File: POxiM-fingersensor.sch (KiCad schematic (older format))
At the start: 6 parts, among them J1 To LED board, J2 To photodiode board, J3 To readout unit

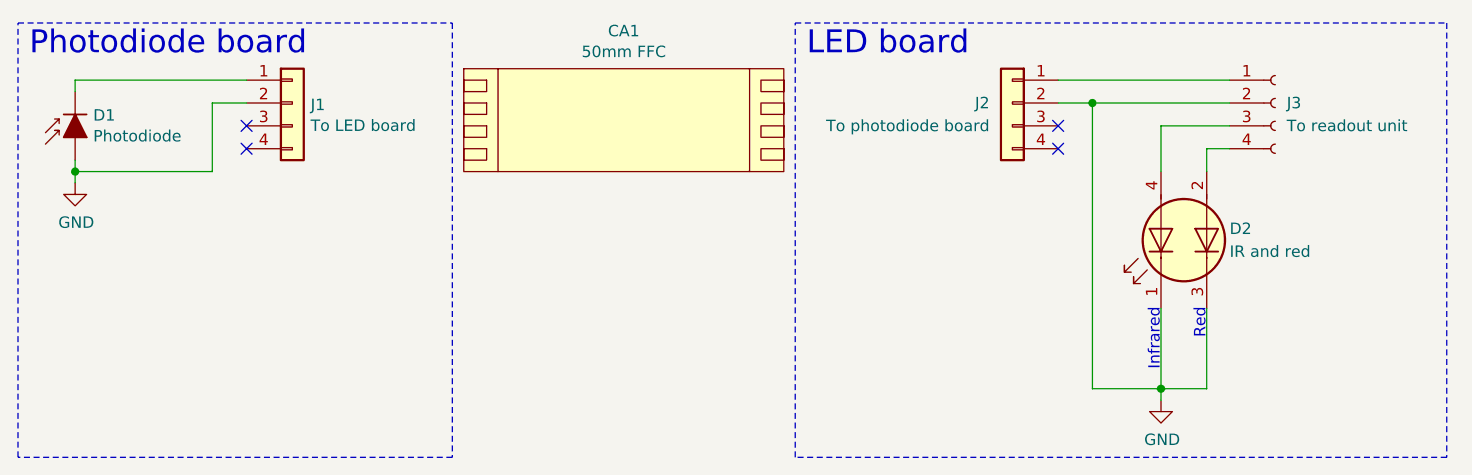
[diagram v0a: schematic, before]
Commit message: Move to flelex layout
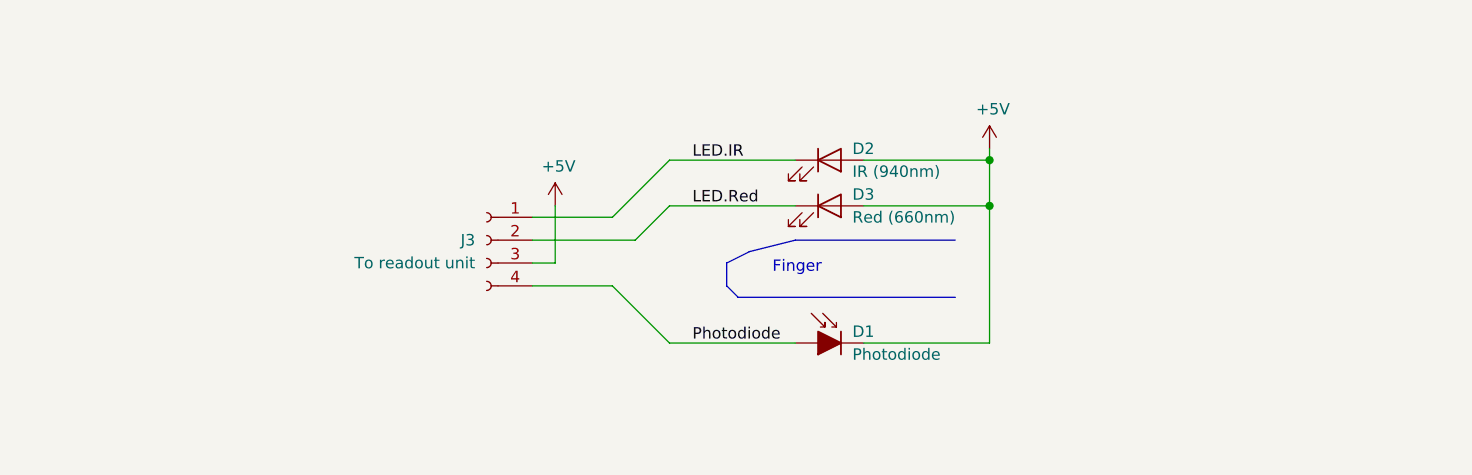
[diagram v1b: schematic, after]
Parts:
- removed CA1: 50mm FFC, POxiM-uncategorised:Accesory, symbol POxiM-mechanical:Premo-Flex_4C
- removed D2: IR and red, POxiM-uncategorised:VSMD66694, symbol POxiM-uncategorised:LED_Dual_AACC
- removed J1: To LED board, POxiM-uncategorised:Molex_200528-0040_1x04-1MP_P1.00mm_Horizontal, symbol Connector_Generic:Conn_01x04
- removed J2: To photodiode board, POxiM-uncategorised:Molex_200528-0040_1x04-1MP_P1.00mm_Horizontal, symbol Connector_Generic:Conn_01x04
- added D2: IR (940nm), LED_SMD:LED_0805_2012Metric, symbol Device:LED
- added D3: Red (660nm), LED_SMD:LED_0805_2012Metric, symbol Device:LED
- J3: footprint POxiM-uncategorised:Molex-Nanofit-4 -> POxiM-uncategorised:Finger-CableConnection; Link https://nl.mouser.com/ProductDetail/Molex/105430-1204?utm_t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 -> (none); Link 2 https://nl.farnell.com/molex/105430-1104/nano-fit-hdr-smt-r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 -> (none); Notes Mouser gold plating, Farnell tin plating -> (none); Order number 538-105430-1204 -> (none); Order number 2 3225233 -> (none); Part number 1054301204 -> (none); Part number 2 105430-1104 -> (none); Supplier Mouser -> (none); Supplier 2 Farnell -> (none)
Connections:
- net LED.IR: now reaches J3.1 (Pin_1)
- net LED.IR: now also D2.1 (K)
- net +5V: now reaches D1.1 (K)
- net +5V: now also J3.3 (Pin_3), D2.2 (A), D3.2 (A)
- net Photodiode: now reaches J3.4 (Pin_4)
- net Photodiode: now also D1.2 (A)
- net GND renamed LED.Red
- net LED.Red: now also D3.1 (K); no longer D1.2 (A)
- no-connect marks 4 -> 0
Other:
- note added: "Finger"
- note removed: "Infrared"
- note removed: "LED board"
- note removed: "Photodiode board"
- note removed: "Red"
- moved on the sheet: D1, J3

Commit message: Export rev F
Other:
- note added: "- Add fudicials\n - Cable connections should have holes in pads\n - Flex part needs to be hatched & no silkscreen\n - Each rigid part needs two 2mm tool holes\n - 0603/0805 agnostic footprints can be used\n - PCB should be less tall\n - Cable connections should be next to LEDs instead of above"
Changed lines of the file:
@@
 Text Label 5800 4450 0    50   ~ 0
 Photodiode
+Text Notes 3150 2550 0    50   ~ 0
+ - Add fudicials\n - Cable connections should have holes in pads\n - Flex part needs to be hatched & no silkscreen\n - Each rigid part needs two 2mm tool holes\n - 0603/0805 agnostic footprints can be used\n - PCB should be less tall\n - Cable connections should be next to LEDs instead of above
 $EndSCHEMATC

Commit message: Rev G
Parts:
- added FID1, FID2, FID3, FID4: Fiducial, Fiducial:Fiducial_0.5mm_Mask1mm, symbol Mechanical:Fiducial
- added H1, H2, H3, H4: M2 alignment hole, MountingHole:MountingHole_2.2mm_M2, symbol Mechanical:MountingHole
- D1: footprint LED_SMD:LED_1206_3216Metric_Castellated -> POxiM-uncategorised:LED_1206_3216Metric_0805_2012Metric_Castellated
- D2, D3: footprint LED_SMD:LED_0805_2012Metric -> POxiM-uncategorised:LED_0805_2012Metric_0603_1608Metric
- J3: Notes (none) -> NOT ON BOM!
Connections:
- net LED.IR: now also D2.2 (A), J3.2 (Pin_2); no longer D2.1 (K), J3.1 (Pin_1)
- net LED.Red: now also D3.2 (A), J3.1 (Pin_1); no longer D3.1 (K), J3.2 (Pin_2)
- net Photodiode: now also D1.1 (K); no longer D1.2 (A)
- removed net +5V: D1.1 (K), D2.2 (A), D3.2 (A), J3.3 (Pin_3)
- new net GND: D1.2 (A), D2.1 (K), D3.1 (K), J3.3 (Pin_3)
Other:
- moved on the sheet: D2, D3
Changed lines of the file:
@@
 L Device:D_Photo_ALT D1
 U 1 1 5EA6D793
-P 6350 4450
-F 0 "D1" H 6200 4500 50  0000 R CNN
-F 1 "Photodiode" H 6200 4400 50  0000 R CNN
-F 2 "LED_SMD:LED_1206_3216Metric_Castellated" H 6300 4450 50  0001 C CNN
-F 3 "${KIPRJMOD}/Datasheets/2711852.pdf" H 6300 4450 50  0001 C CNN
-F 4 "SFH 2701" V 6350 4450 50  0001 C CNN "Part number"
-F 5 "2981719" V 6350 4450 50  0001 C CNN "Order number"
-F 6 "Farnell" V 6350 4450 50  0001 C CNN "Supplier"
-F 7 "" V 6350 4450 50  0001 C CNN "Notes"
-F 8 "https://nl.farnell.com/osram-opto-semiconductors/sfh-2701/photo-diode-820nm-1206/dp/2981719" V 6350 4450 50  0001 C CNN "Link"
-	1    6350 4450
-	-1   0    0    -1
+P 6450 4450
+F 0 "D1" H 6550 4500 50  0000 L CNN
+F 1 "Photodiode" H 6550 4400 50  0000 L CNN
+F 2 "POxiM-uncategorised:LED_1206_3216Metric_0805_2012Metric_Castellated" H 6400 4450 50  0001 C CNN
+F 3 "${KIPRJMOD}/Datasheets/2711852.pdf" H 6400 4450 50  0001 C CNN
+F 4 "SFH 2701" V 6450 4450 50  0001 C CNN "Part number"
+F 5 "2981719" V 6450 4450 50  0001 C CNN "Order number"
+F 6 "Farnell" V 6450 4450 50  0001 C CNN "Supplier"
+F 7 "https://nl.farnell.com/osram-opto-semiconductors/sfh-2701/photo-diode-820nm-1206/dp/2981719" V 6450 4450 50  0001 C CNN "Link"
+	1    6450 4450
+	1    0    0    -1
 $EndComp
 $Comp
@@
 F 2 "POxiM-uncategorised:Finger-CableConnection" H 4900 4000 50  0001 C CNN
 F 3 "~" H 4900 4000 50  0001 C CNN
+F 4 "~" H 0   0   50  0001 C CNN "Link"
+F 5 "NOT ON BOM!" H 0   0   50  0001 C CNN "Notes"
+F 6 "~" H 0   0   50  0001 C CNN "Order number"
+F 7 "~" H 0   0   50  0001 C CNN "Part number"
+F 8 "~" H 0   0   50  0001 C CNN "Supplier"
 	1    4900 4000
 	-1   0    0    -1
@@
 L Device:LED D3
 U 1 1 5EE0E1BF
-P 6400 3850
-F 0 "D3" H 6500 3900 50  0000 L CNN
-F 1 "Red (660nm)" H 6500 3800 50  0000 L CNN
-F 2 "LED_SMD:LED_0805_2012Metric" H 6400 3850 50  0001 C CNN
-F 3 "~" H 6400 3850 50  0001 C CNN
-	1    6400 3850
-	1    0    0    -1
+P 6400 3650
+F 0 "D3" H 6200 3700 50  0000 R CNN
+F 1 "Red (660nm)" H 6200 3600 50  0000 R CNN
+F 2 "POxiM-uncategorised:LED_0805_2012Metric_0603_1608Metric" H 6400 3650 50  0001 C CNN
+F 3 "~" H 6400 3650 50  0001 C CNN
+F 4 "~" H 0   -200 50  0001 C CNN "Link"
+F 5 "~" H 0   -200 50  0001 C CNN "Order number"
+F 6 "~" H 0   -200 50  0001 C CNN "Part number"
+F 7 "~" H 0   -200 50  0001 C CNN "Supplier"
+	1    6400 3650
+	-1   0    0    -1
 $EndComp
 $Comp
 L Device:LED D2
 U 1 1 5EE0E711
-P 6400 3650
-F 0 "D2" H 6500 3700 50  0000 L CNN
-F 1 "IR (940nm)" H 6500 3600 50  0000 L CNN
-F 2 "LED_SMD:LED_0805_2012Metric" H 6400 3650 50  0001 C CNN
-F 3 "~" H 6400 3650 50  0001 C CNN
-	1    6400 3650
-	1    0    0    -1
+P 6400 3850
+F 0 "D2" H 6200 3900 50  0000 R CNN
+F 1 "IR (940nm)" H 6200 3800 50  0000 R CNN
+F 2 "POxiM-uncategorised:LED_0805_2012Metric_0603_1608Metric" H 6400 3850 50  0001 C CNN
+F 3 "~" H 6400 3850 50  0001 C CNN
+F 4 "~" H 0   200 50  0001 C CNN "Link"
+F 5 "~" H 0   200 50  0001 C CNN "Order number"
+F 6 "~" H 0   200 50  0001 C CNN "Part number"
+F 7 "~" H 0   200 50  0001 C CNN "Supplier"
+	1    6400 3850
+	-1   0    0    -1
 $EndComp
 Wire Bus Line
@@
 Wire Wire Line
 	5700 4450 6250 4450
-$Comp
-L power:+5V #PWR0101
-U 1 1 5EE147B5
-P 5200 3850
-F 0 "#PWR0101" H 5200 3700 50  0001 C CNN
-F 1 "+5V" H 5215 4023 50  0000 C CNN
-F 2 "" H 5200 3850 50  0001 C CNN
-F 3 "" H 5200 3850 50  0001 C CNN
-	1    5200 3850
-	1    0    0    -1
-$EndComp
 Wire Wire Line
 	5100 4100 5200 4100
 Wire Wire Line
-	5200 4100 5200 3850
-$Comp
-L power:+5V #PWR0102
-U 1 1 5EE15AC6
-P 7100 3600
-F 0 "#PWR0102" H 7100 3450 50  0001 C CNN
-F 1 "+5V" H 7115 3773 50  0000 C CNN
-F 2 "" H 7100 3600 50  0001 C CNN
-F 3 "" H 7100 3600 50  0001 C CNN
-	1    7100 3600
-	1    0    0    -1
-$EndComp
-Wire Wire Line
-	6550 3650 7100 3650
-Wire Wire Line
-	7100 3650 7100 3850
-Wire Wire Line
-	7100 4450 6550 4450
-Wire Wire Line
-	6550 3850 7100 3850
-Connection ~ 7100 3850
-Wire Wire Line
-	7100 3850 7100 4450
-Wire Wire Line
-	7100 3600 7100 3650
-Connection ~ 7100 3650
+	6550 3650 7200 3650
+Wire Wire Line
+	7200 3650 7200 3850
+Wire Wire Line
+	7200 4450 6550 4450
+Wire Wire Line
+	6550 3850 7200 3850
+Connection ~ 7200 3850
+Wire Wire Line
+	7200 3850 7200 4450
+Text Label 5800 3850 0    50   ~ 0
+LED.IR
 Text Label 5800 3650 0    50   ~ 0
-LED.IR
-Text Label 5800 3850 0    50   ~ 0
 LED.Red
 Text Label 5800 4450 0    50   ~ 0
@@
 Text Notes 3150 2550 0    50   ~ 0
  - Add fudicials\n - Cable connections should have holes in pads\n - Flex part needs to be hatched & no silkscreen\n - Each rigid part needs two 2mm tool holes\n - 0603/0805 agnostic footprints can be used\n - PCB should be less tall\n - Cable connections should be next to LEDs instead of above
+$Comp
+L power:GND #PWR0101
+U 1 1 5F046C3E
+P 5200 4250
+F 0 "#PWR0101" H 5200 4000 50  0001 C CNN
+F 1 "GND" H 5205 4077 50  0000 C CNN
+F 2 "" H 5200 4250 50  0001 C CNN
+F 3 "" H 5200 4250 50  0001 C CNN
+	1    5200 4250
+	1    0    0    -1
+$EndComp
+Wire Wire Line
+	5200 4250 5200 4100
+$Comp
+L power:GND #PWR0102
+U 1 1 5F047B9A
+P 7200 4500
+F 0 "#PWR0102" H 7200 4250 50  0001 C CNN
+F 1 "GND" H 7205 4327 50  0000 C CNN
+F 2 "" H 7200 4500 50  0001 C CNN
+F 3 "" H 7200 4500 50  0001 C CNN
+	1    7200 4500
+	1    0    0    -1
+$EndComp
+Wire Wire Line
+	7200 4500 7200 4450
+Connection ~ 7200 4450
+$Comp
+L Mechanical:MountingHole H1
+U 1 1 5F048FBF
+P 1250 7200
+F 0 "H1" H 1350 7246 50  0000 L CNN
+F 1 "M2 alignment hole" H 1350 7155 50  0000 L CNN
+F 2 "MountingHole:MountingHole_2.2mm_M2" H 1250 7200 50  0001 C CNN
+F 3 "~" H 1250 7200 50  0001 C CNN
+F 4 "~" H 1250 7200 50  0001 C CNN "Part number"
+F 5 "~" H 1250 7200 50  0001 C CNN "Order number"
+F 6 "~" H 1250 7200 50  0001 C CNN "Supplier"
+F 7 "NOT ON BOM!" H 1250 7200 50  0001 C CNN "Notes"
+F 8 "~" H 1250 7200 50  0001 C CNN "Link"
+	1    1250 7200
+	1    0    0    -1
+$EndComp
+$Comp
+L Mechanical:MountingHole H2
+U 1 1 5F049620
+P 1250 7450
+F 0 "H2" H 1350 7496 50  0000 L CNN
+F 1 "M2 alignment hole" H 1350 7405 50  0000 L CNN
+F 2 "MountingHole:MountingHole_2.2mm_M2" H 1250 7450 50  0001 C CNN
+F 3 "~" H 1250 7450 50  0001 C CNN
+F 4 "~" H 1250 7450 50  0001 C CNN "Part number"
+F 5 "~" H 1250 7450 50  0001 C CNN "Order number"
+F 6 "~" H 1250 7450 50  0001 C CNN "Supplier"
+F 7 "NOT ON BOM!" H 1250 7450 50  0001 C CNN "Notes"
+F 8 "~" H 1250 7450 50  0001 C CNN "Link"
+	1    1250 7450
+	1    0    0    -1
+$EndComp
+$Comp
+L Mechanical:MountingHole H3
+U 1 1 5F049B3D
+P 2250 7200
+F 0 "H3" H 2350 7246 50  0000 L CNN
+F 1 "M2 alignment hole" H 2350 7155 50  0000 L CNN
+F 2 "MountingHole:MountingHole_2.2mm_M2" H 2250 7200 50  0001 C CNN
+F 3 "~" H 2250 7200 50  0001 C CNN
+F 4 "~" H 2250 7200 50  0001 C CNN "Part number"
+F 5 "~" H 2250 7200 50  0001 C CNN "Order number"
+F 6 "~" H 2250 7200 50  0001 C CNN "Supplier"
+F 7 "NOT ON BOM!" H 2250 7200 50  0001 C CNN "Notes"
+F 8 "~" H 2250 7200 50  0001 C CNN "Link"
+	1    2250 7200
+	1    0    0    -1
+$EndComp
+$Comp
+L Mechanical:MountingHole H4
+U 1 1 5F04A2B3
+P 2250 7450
+F 0 "H4" H 2350 7496 50  0000 L CNN
+F 1 "M2 alignment hole" H 2350 7405 50  0000 L CNN
+F 2 "MountingHole:MountingHole_2.2mm_M2" H 2250 7450 50  0001 C CNN
+F 3 "~" H 2250 7450 50  0001 C CNN
+F 4 "~" H 2250 7450 50  0001 C CNN "Part number"
+F 5 "~" H 2250 7450 50  0001 C CNN "Order number"
+F 6 "~" H 2250 7450 50  0001 C CNN "Supplier"
+F 7 "NOT ON BOM!" H 2250 7450 50  0001 C CNN "Notes"
+F 8 "~" H 2250 7450 50  0001 C CNN "Link"
+	1    2250 7450
+	1    0    0    -1
+$EndComp
+$Comp
+L Mechanical:Fiducial FID1
+U 1 1 5F04B929
+P 3250 7200
+F 0 "FID1" H 3335 7246 50  0000 L CNN
+F 1 "Fiducial" H 3335 7155 50  0000 L CNN
+F 2 "Fiducial:Fiducial_0.5mm_Mask1mm" H 3250 7200 50  0001 C CNN
+F 3 "~" H 3250 7200 50  0001 C CNN
+F 4 "~" H 0   0   50  0001 C CNN "Link"
+F 5 "NOT ON BOM!" H 0   0   50  0001 C CNN "Notes"
+F 6 "~" H 0   0   50  0001 C CNN "Order number"
+F 7 "~" H 0   0   50  0001 C CNN "Part number"
+F 8 "~" H 0   0   50  0001 C CNN "Supplier"
+	1    3250 7200
+	1    0    0    -1
+$EndComp
+$Comp
+L Mechanical:Fiducial FID2
+U 1 1 5F04C457
+P 3250 7450
+F 0 "FID2" H 3335 7496 50  0000 L CNN
+F 1 "Fiducial" H 3335 7405 50  0000 L CNN
+F 2 "Fiducial:Fiducial_0.5mm_Mask1mm" H 3250 7450 50  0001 C CNN
+F 3 "~" H 3250 7450 50  0001 C CNN
+F 4 "~" H 0   0   50  0001 C CNN "Link"
+F 5 "NOT ON BOM!" H 0   0   50  0001 C CNN "Notes"
+F 6 "~" H 0   0   50  0001 C CNN "Order number"
+F 7 "~" H 0   0   50  0001 C CNN "Part number"
+F 8 "~" H 0   0   50  0001 C CNN "Supplier"
+	1    3250 7450
+	1    0    0    -1
+$EndComp
+$Comp
+L Mechanical:Fiducial FID3
+U 1 1 5F04D55D
+P 3850 7200
+F 0 "FID3" H 3935 7246 50  0000 L CNN
+F 1 "Fiducial" H 3935 7155 50  0000 L CNN
+F 2 "Fiducial:Fiducial_0.5mm_Mask1mm" H 3850 7200 50  0001 C CNN
+F 3 "~" H 3850 7200 50  0001 C CNN
+F 4 "~" H 0   0   50  0001 C CNN "Link"
+F 5 "NOT ON BOM!" H 0   0   50  0001 C CNN "Notes"
+F 6 "~" H 0   0   50  0001 C CNN "Order number"
+F 7 "~" H 0   0   50  0001 C CNN "Part number"
+F 8 "~" H 0   0   50  0001 C CNN "Supplier"
+	1    3850 7200
+	1    0    0    -1
+$EndComp
+$Comp
+L Mechanical:Fiducial FID4
+U 1 1 5F04D563
+P 3850 7450
+F 0 "FID4" H 3935 7496 50  0000 L CNN
+F 1 "Fiducial" H 3935 7405 50  0000 L CNN
+F 2 "Fiducial:Fiducial_0.5mm_Mask1mm" H 3850 7450 50  0001 C CNN
+F 3 "~" H 3850 7450 50  0001 C CNN
+F 4 "~" H 0   0   50  0001 C CNN "Link"
+F 5 "NOT ON BOM!" H 0   0   50  0001 C CNN "Notes"
+F 6 "~" H 0   0   50  0001 C CNN "Order number"
+F 7 "~" H 0   0   50  0001 C CNN "Part number"
+F 8 "~" H 0   0   50  0001 C CNN "Supplier"
+	1    3850 7450
+	1    0    0    -1
+$EndComp
 $EndSCHEMATC

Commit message: Rev I
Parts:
- FID1, FID2, FID3, FID4: footprint Fiducial:Fiducial_0.5mm_Mask1mm -> POxiM-uncategorised:Fiducial_1mm_Mask2mm
- H1, H2, H3, H4: footprint MountingHole:MountingHole_2.2mm_M2 -> POxiM-uncategorised:AlignmentHole_2mm
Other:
- note added: "- Update footprints\n- Tool holes to 2mm\n- Routing posts can extend past board edge\n- Increase fiducial size"
- note removed: "- Add fudicials\n - Cable connections should have holes in pads\n - Flex part needs to be hatched & no silkscreen\n - Each rigid part needs two 2mm tool holes\n - 0603/0805 agnostic footprints can be used\n - PCB should be less tall\n - Cable connections should be next to LEDs instead of above"
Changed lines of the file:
@@
 Photodiode
 Text Notes 3150 2550 0    50   ~ 0
- - Add fudicials\n - Cable connections should have holes in pads\n - Flex part needs to be hatched & no silkscreen\n - Each rigid part needs two 2mm tool holes\n - 0603/0805 agnostic footprints can be used\n - PCB should be less tall\n - Cable connections should be next to LEDs instead of above
+- Update footprints\n- Tool holes to 2mm\n- Routing posts can extend past board edge\n- Increase fiducial size
 $Comp
 L power:GND #PWR0101
@@
 F 0 "H1" H 1350 7246 50  0000 L CNN
 F 1 "M2 alignment hole" H 1350 7155 50  0000 L CNN
-F 2 "MountingHole:MountingHole_2.2mm_M2" H 1250 7200 50  0001 C CNN
+F 2 "POxiM-uncategorised:AlignmentHole_2mm" H 1250 7200 50  0001 C CNN
 F 3 "~" H 1250 7200 50  0001 C CNN
 F 4 "~" H 1250 7200 50  0001 C CNN "Part number"
@@
 F 0 "H2" H 1350 7496 50  0000 L CNN
 F 1 "M2 alignment hole" H 1350 7405 50  0000 L CNN
-F 2 "MountingHole:MountingHole_2.2mm_M2" H 1250 7450 50  0001 C CNN
+F 2 "POxiM-uncategorised:AlignmentHole_2mm" H 1250 7450 50  0001 C CNN
 F 3 "~" H 1250 7450 50  0001 C CNN
 F 4 "~" H 1250 7450 50  0001 C CNN "Part number"
@@
 F 0 "H3" H 2350 7246 50  0000 L CNN
 F 1 "M2 alignment hole" H 2350 7155 50  0000 L CNN
-F 2 "MountingHole:MountingHole_2.2mm_M2" H 2250 7200 50  0001 C CNN
+F 2 "POxiM-uncategorised:AlignmentHole_2mm" H 2250 7200 50  0001 C CNN
 F 3 "~" H 2250 7200 50  0001 C CNN
 F 4 "~" H 2250 7200 50  0001 C CNN "Part number"
@@
 F 0 "H4" H 2350 7496 50  0000 L CNN
 F 1 "M2 alignment hole" H 2350 7405 50  0000 L CNN
-F 2 "MountingHole:MountingHole_2.2mm_M2" H 2250 7450 50  0001 C CNN
+F 2 "POxiM-uncategorised:AlignmentHole_2mm" H 2250 7450 50  0001 C CNN
 F 3 "~" H 2250 7450 50  0001 C CNN
 F 4 "~" H 2250 7450 50  0001 C CNN "Part number"
@@
 F 0 "FID1" H 3335 7246 50  0000 L CNN
 F 1 "Fiducial" H 3335 7155 50  0000 L CNN
-F 2 "Fiducial:Fiducial_0.5mm_Mask1mm" H 3250 7200 50  0001 C CNN
+F 2 "POxiM-uncategorised:Fiducial_1mm_Mask2mm" H 3250 7200 50  0001 C CNN
 F 3 "~" H 3250 7200 50  0001 C CNN
 F 4 "~" H 0   0   50  0001 C CNN "Link"
@@
 F 0 "FID2" H 3335 7496 50  0000 L CNN
 F 1 "Fiducial" H 3335 7405 50  0000 L CNN
-F 2 "Fiducial:Fiducial_0.5mm_Mask1mm" H 3250 7450 50  0001 C CNN
+F 2 "POxiM-uncategorised:Fiducial_1mm_Mask2mm" H 3250 7450 50  0001 C CNN
 F 3 "~" H 3250 7450 50  0001 C CNN
 F 4 "~" H 0   0   50  0001 C CNN "Link"
@@
 F 0 "FID3" H 3935 7246 50  0000 L CNN
 F 1 "Fiducial" H 3935 7155 50  0000 L CNN
-F 2 "Fiducial:Fiducial_0.5mm_Mask1mm" H 3850 7200 50  0001 C CNN
+F 2 "POxiM-uncategorised:Fiducial_1mm_Mask2mm" H 3850 7200 50  0001 C CNN
 F 3 "~" H 3850 7200 50  0001 C CNN
 F 4 "~" H 0   0   50  0001 C CNN "Link"
@@
 F 0 "FID4" H 3935 7496 50  0000 L CNN
 F 1 "Fiducial" H 3935 7405 50  0000 L CNN
-F 2 "Fiducial:Fiducial_0.5mm_Mask1mm" H 3850 7450 50  0001 C CNN
+F 2 "POxiM-uncategorised:Fiducial_1mm_Mask2mm" H 3850 7450 50  0001 C CNN
 F 3 "~" H 3850 7450 50  0001 C CNN
 F 4 "~" H 0   0   50  0001 C CNN "Link"

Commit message: Rev J
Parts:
- D1: Link https://nl.farnell.com/osram-opto-semiconductors/sfh-2701/p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 -> https://nl.mouser.com/ProductDetail/OSRAM-Opto-Semiconducto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; Order number 2981719 -> 720-SFH2701; Supplier Farnell -> Mouser
- D2: Link (none) -> https://nl.mouser.com/ProductDetail/604-APTD2012F3C; Order number (none) -> 604-APTD2012F3C; Part number (none) -> APTD2012F3C; Supplier (none) -> Mouser
- D3: Link (none) -> https://nl.mouser.com/ProductDetail/Lumex/SML-LX0603SRW-TR?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; Order number (none) -> 696-SML-LX0603SRW; Part number (none) -> SML-LX0603SRW-TR; Supplier (none) -> Mouser
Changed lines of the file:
@@
 F 3 "${KIPRJMOD}/Datasheets/2711852.pdf" H 6400 4450 50  0001 C CNN
 F 4 "SFH 2701" V 6450 4450 50  0001 C CNN "Part number"
-F 5 "2981719" V 6450 4450 50  0001 C CNN "Order number"
-F 6 "Farnell" V 6450 4450 50  0001 C CNN "Supplier"
-F 7 "https://nl.farnell.com/osram-opto-semiconductors/sfh-2701/photo-diode-820nm-1206/dp/2981719" V 6450 4450 50  0001 C CNN "Link"
+F 5 "720-SFH2701" V 6450 4450 50  0001 C CNN "Order number"
+F 6 "Mouser" V 6450 4450 50  0001 C CNN "Supplier"
+F 7 "https://nl.mouser.com/ProductDetail/OSRAM-Opto-Semiconductors/SFH-2701?qs=%2Fha2pyFadujkohCJnotANpZPDvUKMp5%2FTRZ67%252BHfjgI%3D" V 6450 4450 50  0001 C CNN "Link"
 	1    6450 4450
 	1    0    0    -1
@@
 F 1 "Red (660nm)" H 6200 3600 50  0000 R CNN
 F 2 "POxiM-uncategorised:LED_0805_2012Metric_0603_1608Metric" H 6400 3650 50  0001 C CNN
-F 3 "~" H 6400 3650 50  0001 C CNN
-F 4 "~" H 0   -200 50  0001 C CNN "Link"
-F 5 "~" H 0   -200 50  0001 C CNN "Order number"
-F 6 "~" H 0   -200 50  0001 C CNN "Part number"
-F 7 "~" H 0   -200 50  0001 C CNN "Supplier"
+F 3 "${KIPRJMOD}/Datasheets/SML-LX0603SRW-TR-1135914.pdf" H 6400 3650 50  0001 C CNN
+F 4 "https://nl.mouser.com/ProductDetail/Lumex/SML-LX0603SRW-TR?qs=I1ILoAvtKy93HVCzWwpawA%3D%3D" H 0   -200 50  0001 C CNN "Link"
+F 5 "696-SML-LX0603SRW" H 0   -200 50  0001 C CNN "Order number"
+F 6 "SML-LX0603SRW-TR" H 0   -200 50  0001 C CNN "Part number"
+F 7 "Mouser" H 0   -200 50  0001 C CNN "Supplier"
 	1    6400 3650
 	-1   0    0    -1
@@
 F 1 "IR (940nm)" H 6200 3800 50  0000 R CNN
 F 2 "POxiM-uncategorised:LED_0805_2012Metric_0603_1608Metric" H 6400 3850 50  0001 C CNN
-F 3 "~" H 6400 3850 50  0001 C CNN
-F 4 "~" H 0   200 50  0001 C CNN "Link"
-F 5 "~" H 0   200 50  0001 C CNN "Order number"
-F 6 "~" H 0   200 50  0001 C CNN "Part number"
-F 7 "~" H 0   200 50  0001 C CNN "Supplier"
+F 3 "${KIPRJMOD}/Datasheets/APTD2012F3C-1388795.pdf" H 6400 3850 50  0001 C CNN
+F 4 "https://nl.mouser.com/ProductDetail/604-APTD2012F3C" H 0   200 50  0001 C CNN "Link"
+F 5 "604-APTD2012F3C" H 0   200 50  0001 C CNN "Order number"
+F 6 "APTD2012F3C" H 0   200 50  0001 C CNN "Part number"
+F 7 "Mouser" H 0   200 50  0001 C CNN "Supplier"
 	1    6400 3850
 	-1   0    0    -1
